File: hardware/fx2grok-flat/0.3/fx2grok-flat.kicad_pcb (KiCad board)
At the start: 4 copper layers, 34.9 x 16 mm, 36 parts, among them IC1 CY7C68013A-56, J1 Conn, P1 pkl_USB_OTG, U1 3.3V, U2 USBLC6-2, U3 IP425x-4-TTL, U4 IP425x-4-TTL, U5 24LC00, U6 IP425x-4-TTL, X1 24MHz

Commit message: Added 3d models to the board file.
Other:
- board text added: "1BitSquared"

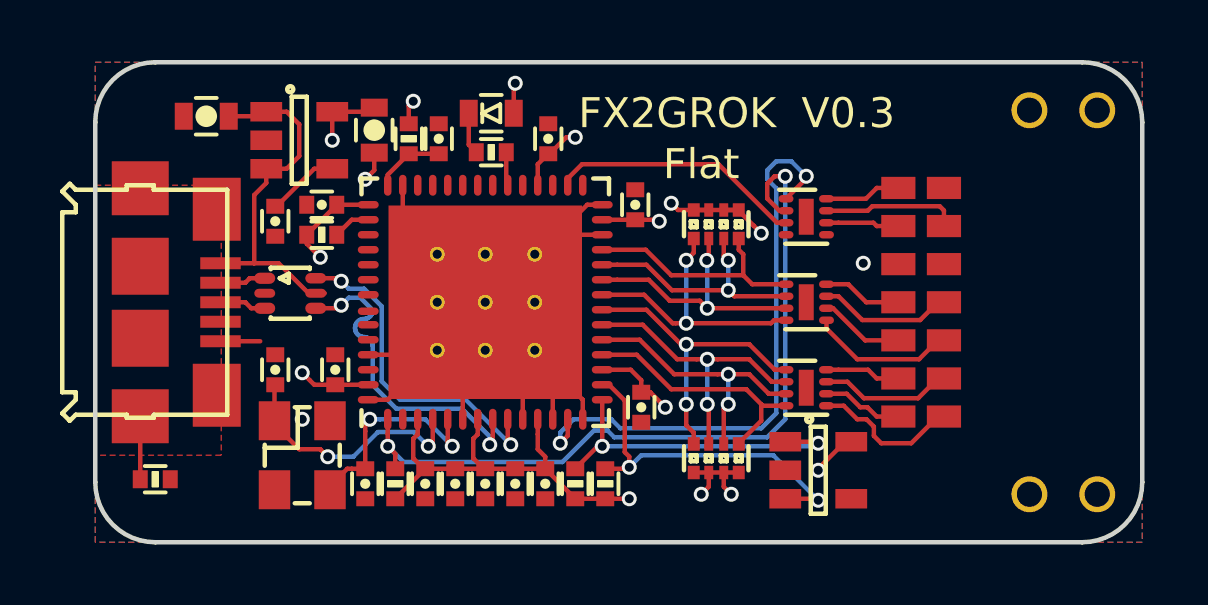
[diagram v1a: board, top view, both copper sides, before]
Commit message: Moved config flash to clean up PB0 trace.
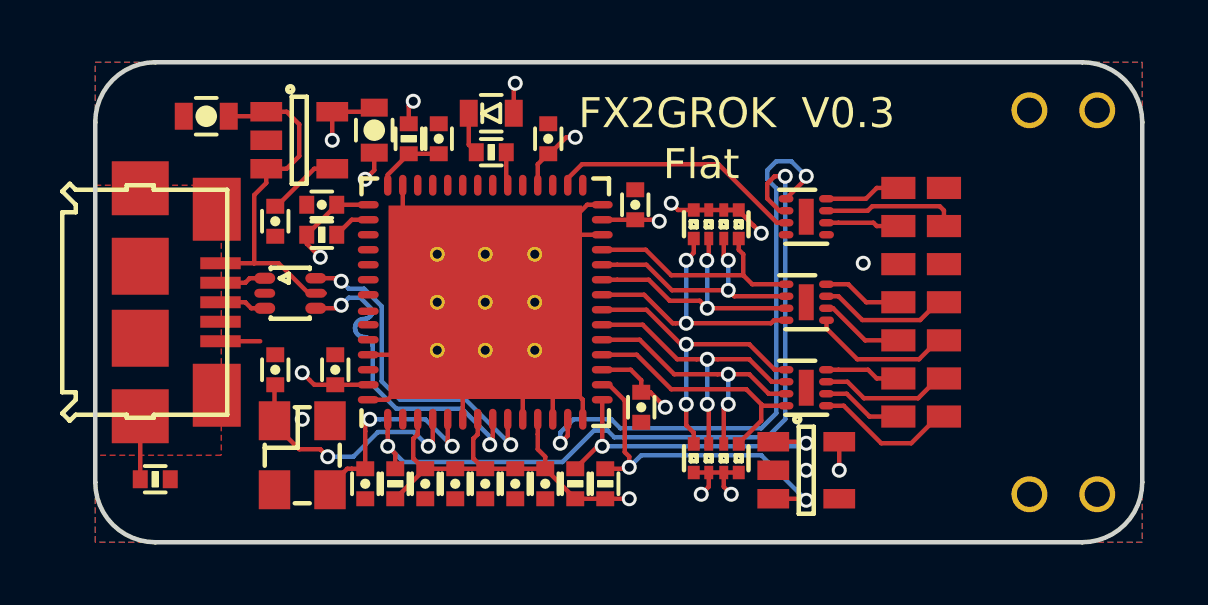
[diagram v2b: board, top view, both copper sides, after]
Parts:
- added REF**: 1b2_Logo_SilkS_10mm, pkl_logos:1b2_Logo_SilkS_10mm, B.Cu at (39.5, 30.5)
- moved U5 0.40 mm to (45.7, 35.6)
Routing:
- net +3V3: track 40.7 -> 40.1 mm
- net GND: vias 3 -> 4
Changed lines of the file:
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@@
-(kicad_pcb (version 20171130) (host pcbnew 5.0.0-rc2-dev-unknown-0d8692d~64~ubuntu16.04.1)
+(kicad_pcb (version 20171130) (host pcbnew 5.0.0-rc2-dev-unknown-268aeeb~64~ubuntu16.04.1)
   (general
     (thickness 1.6)
     (drawings 46)
-    (tracks 438)
+    (tracks 431)
     (zones 0)
-    (modules 36)
+    (modules 37)
     (nets 62)
   )
@@
     (add_net "Net-(U5-Pad4)")
   )
+  (module pkl_logos:1b2_Logo_SilkS_10mm locked (layer B.Cu)
+    (at 39.5 30.5 90)
+    (fp_text reference REF** (at 0 -6 90) (layer B.Fab)
+      (effects (font (size 1 1) (thickness 0.15)) (justify mirror))
+    )
+    (fp_text value 1b2_Logo_SilkS_10mm (at 0 6.35 90) (layer B.Fab)
+      (effects (font (size 1 1) (thickness 0.15)) (justify mirror))
+    )
+    (fp_line (start -1 1) (end -1 5) (layer B.SilkS) (width 0.4))
+    (fp_line (start -1 5) (end -5 5) (layer B.SilkS) (width 0.4))
+    (fp_line (start -5 5) (end -5 1) (layer B.SilkS) (width 0.4))
+    (fp_line (start -5 1) (end -1 1) (layer B.SilkS) (width 0.4))
+    (fp_line (start -1 5) (end 0 4) (layer B.SilkS) (width 0.4))
+    (fp_line (start 0 4) (end 0 0) (layer B.SilkS) (width 0.4))
+    (fp_line (start 0 0) (end -1 1) (layer B.SilkS) (width 0.4))
+    (fp_line (start -5 1) (end -4 0) (layer B.SilkS) (width 0.4))
+    (fp_line (start -4 0) (end 0 0) (layer B.SilkS) (width 0.4))
+    (fp_line (start 4 4) (end 1 4) (layer B.SilkS) (width 0.4))
+    (fp_line (start 1 4) (end 1 -1) (layer B.SilkS) (width 0.4))
+    (fp_line (start 1 -1) (end -4 -1) (layer B.SilkS) (width 0.4))
+    (fp_line (start -4 -1) (end -4 -4) (layer B.SilkS) (width 0.4))
+    (fp_line (start -4 -4) (end 4 -4) (layer B.SilkS) (width 0.4))
+    (fp_line (start 4 -4) (end 4 4) (layer B.SilkS) (width 0.4))
+    (fp_line (start 4 4) (end 5 3) (layer B.SilkS) (width 0.4))
+    (fp_line (start 5 3) (end 5 -5) (layer B.SilkS) (width 0.4))
+    (fp_line (start 5 -5) (end 4 -4) (layer B.SilkS) (width 0.4))
+    (fp_line (start -4 -4) (end -3 -5) (layer B.SilkS) (width 0.4))
+    (fp_line (start -3 -5) (end 5 -5) (layer B.SilkS) (width 0.4))
+  )
   (module pkl_samtec:TFM-107-02-x-DH locked (layer F.Cu)
     (at 55.4 30 270)
@@
   )
   (module pkl_housings_sot:SOT-23-5 (layer F.Cu)
-    (at 46.1 35.6 180)
+    (at 45.7 35.6 180)
     (descr "5-pin SOT23 package")
     (tags SOT-23-5)
@@
   (segment (start 42.45 26.925) (end 41.425004 26.925) (width 0.15) (layer F.Cu) (net 1))
   (via (at 41.200004 26.7) (size 0.5) (drill 0.3) (layers F.Cu B.Cu) (net 1))
-  (segment (start 47.2 34.65) (end 46.995 34.65) (width 0.15) (layer F.Cu) (net 1))
-  (segment (start 46.995 34.65) (end 46.1 35.545) (width 0.15) (layer F.Cu) (net 1))
-  (segment (start 46.1 35.545) (end 46.1 35.6) (width 0.15) (layer F.Cu) (net 1))
-  (via (at 46.1 35.6) (size 0.5) (drill 0.3) (layers F.Cu B.Cu) (net 1))
   (segment (start 39 36.55) (end 39.8 36.55) (width 0.15) (layer F.Cu) (net 1))
   (via (at 39.8 36.55) (size 0.5) (drill 0.3) (layers F.Cu B.Cu) (net 1))
@@
   (segment (start 35.95 22.75) (end 36 22.7) (width 0.15) (layer F.Cu) (net 1))
   (segment (start 35.95 23.7) (end 35.95 22.75) (width 0.15) (layer F.Cu) (net 1))
+  (via (at 46.8 35.6) (size 0.5) (drill 0.3) (layers F.Cu B.Cu) (net 1))
+  (segment (start 46.8 34.65) (end 46.8 35.6) (width 0.15) (layer F.Cu) (net 1))
   (segment (start 31.3 25.013544) (end 31.3 25.6) (width 0.15) (layer F.Cu) (net 2))
   (segment (start 31.3 25.6) (end 31 25.9) (width 0.15) (layer F.Cu) (net 2))
@@
   (via (at 47.6 28.7) (size 0.5) (drill 0.3) (layers F.Cu B.Cu) (net 2))
   (via (at 28.9 33.9) (size 0.5) (drill 0.3) (layers F.Cu B.Cu) (net 2))
+  (via (at 45.7 35.6) (size 0.5) (drill 0.3) (layers F.Cu B.Cu) (net 2))
   (segment (start 26.175 28.7) (end 27.3 28.7) (width 0.15) (layer F.Cu) (net 3))
   (segment (start 27.3 28.7) (end 28.110715 28.7) (width 0.15) (layer F.Cu) (net 3))
@@
   (segment (start 33.75 33.9) (end 33.75 34.650002) (width 0.15) (layer F.Cu) (net 6))
   (via (at 33.899998 34.8) (size 0.5) (drill 0.3) (layers F.Cu B.Cu) (net 6))
-  (segment (start 45 34.65) (end 46.05 34.65) (width 0.15) (layer F.Cu) (net 7))
-  (segment (start 46.05 34.65) (end 46.1 34.7) (width 0.15) (layer F.Cu) (net 7))
-  (via (at 46.1 34.7) (size 0.5) (drill 0.3) (layers F.Cu B.Cu) (net 7))
+  (segment (start 44.6 34.65) (end 45.65 34.65) (width 0.15) (layer F.Cu) (net 7))
+  (segment (start 45.65 34.65) (end 45.7 34.7) (width 0.15) (layer F.Cu) (net 7))
+  (via (at 45.7 34.7) (size 0.5) (drill 0.3) (layers F.Cu B.Cu) (net 7))
   (segment (start 38.75 34.8) (end 38.9 34.8) (width 0.15) (layer F.Cu) (net 7))
   (segment (start 38.9 33.25) (end 38.9 34.8) (width 0.15) (layer F.Cu) (net 7))
   (via (at 38.9 34.8) (size 0.5) (drill 0.3) (layers F.Cu B.Cu) (net 7))
-  (segment (start 46 34.8) (end 38.9 34.8) (width 0.15) (layer B.Cu) (net 7))
-  (segment (start 46.1 34.7) (end 46 34.8) (width 0.15) (layer B.Cu) (net 7))
   (segment (start 38 35.55) (end 38.75 34.8) (width 0.15) (layer F.Cu) (net 7))
-  (segment (start 46.1 36.6) (end 44.6 35.1) (width 0.15) (layer B.Cu) (net 8))
-  (segment (start 44.6 35.1) (end 40.2 35.1) (width 0.15) (layer B.Cu) (net 8))
-  (segment (start 40.2 35.1) (end 39.8 35.5) (width 0.15) (layer B.Cu) (net 8))
-  (segment (start 45 36.55) (end 46.05 36.55) (width 0.15) (layer F.Cu) (net 8))
-  (segment (start 46.05 36.55) (end 46.1 36.6) (width 0.15) (layer F.Cu) (net 8))
-  (via (at 46.1 36.6) (size 0.5) (drill 0.3) (layers F.Cu B.Cu) (net 8))
+  (segment (start 45.6 34.8) (end 45.7 34.7) (width 0.15) (layer B.Cu) (net 7))
+  (segment (start 38.9 34.8) (end 45.6 34.8) (width 0.15) (layer B.Cu) (net 7))
+  (segment (start 44.6 36.55) (end 45.65 36.55) (width 0.15) (layer F.Cu) (net 8))
+  (via (at 45.7 36.6) (size 0.5) (drill 0.3) (layers F.Cu B.Cu) (net 8))
   (segment (start 39 35.55) (end 39.75 35.55) (width 0.15) (layer F.Cu) (net 8))
   (segment (start 39.75 35.55) (end 39.8 35.5) (width 0.15) (layer F.Cu) (net 8))
@@
   (segment (start 39.8 35.146447) (end 39.8 35.5) (width 0.15) (layer F.Cu) (net 8))
   (via (at 39.8 35.5) (size 0.5) (drill 0.3) (layers F.Cu B.Cu) (net 8))
+  (segment (start 45.65 36.55) (end 45.7 36.6) (width 0.15) (layer F.Cu) (net 8))
+  (segment (start 44.2 35.1) (end 45.7 36.6) (width 0.15) (layer B.Cu) (net 8))
+  (segment (start 40.2 35.1) (end 44.2 35.1) (width 0.15) (layer B.Cu) (net 8))
+  (segment (start 39.8 35.5) (end 40.2 35.1) (width 0.15) (layer B.Cu) (net 8))
   (segment (start 44.2 33.45) (end 44.2 33.4) (width 0.15) (layer F.Cu) (net 9))
   (segment (start 44.2 33.4) (end 43.7 32.9) (width 0.15) (layer F.Cu) (net 9))
@@
   (segment (start 41.95 28.35) (end 41.7 28.6) (width 0.15) (layer F.Cu) (net 18))
   (via (at 41.7 28.6) (size 0.5) (drill 0.3) (layers F.Cu B.Cu) (net 18))
-  (segment (start 47.74 33.5) (end 47.5 33.5) (width 0.15) (layer F.Cu) (net 19))
-  (segment (start 48.05 33.81) (end 47.74 33.5) (width 0.15) (layer F.Cu) (net 19))
   (segment (start 47.05 33.05) (end 46.375 33.05) (width 0.15) (layer F.Cu) (net 19))
-  (segment (start 47.5 33.5) (end 47.05 33.05) (width 0.15) (layer F.Cu) (net 19))
-  (segment (start 48.77 33.81) (end 48.05 33.81) (width 0.15) (layer F.Cu) (net 19))
+  (segment (start 47.81 33.81) (end 47.05 33.05) (width 0.15) (layer F.Cu) (net 19))
+  (segment (start 48.77 33.81) (end 47.81 33.81) (width 0.15) (layer F.Cu) (net 19))
+  (segment (start 46.375 33.45) (end 46.95 33.45) (width 0.15) (layer F.Cu) (net 20))
+  (segment (start 49.2 34.7) (end 50.09 33.81) (width 0.15) (layer F.Cu) (net 20))
   (segment (start 50.09 33.81) (end 50.29 33.81) (width 0.15) (layer F.Cu) (net 20))
+  (segment (start 46.95 33.45) (end 48.2 34.7) (width 0.15) (layer F.Cu) (net 20))
   (segment (start 48.2 34.7) (end 49.2 34.7) (width 0.15) (layer F.Cu) (net 20))
-  (segment (start 47.954001 34.454001) (end 48.2 34.7) (width 0.15) (layer F.Cu) (net 20))
-  (segment (start 47.954001 34.145799) (end 47.954001 34.454001) (width 0.15) (layer F.Cu) (net 20))
-  (segment (start 49.2 34.7) (end 50.09 33.81) (width 0.15) (layer F.Cu) (net 20))
-  (segment (start 46.375 33.45) (end 46.95 33.45) (width 0.15) (layer F.Cu) (net 20))
-  (segment (start 46.95 33.45) (end 47.4 33.9) (width 0.15) (layer F.Cu) (net 20))
-  (segment (start 47.4 33.9) (end 47.708202 33.9) (width 0.15) (layer F.Cu) (net 20))
-  (segment (start 47.708202 33.9) (end 47.954001 34.145799) (width 0.15) (layer F.Cu) (net 20))
   (segment (start 46.775 32.25) (end 46.375 32.25) (width 0.15) (layer F.Cu) (net 21))
   (segment (start 47.76 32.25) (end 46.775 32.25) (width 0.15) (layer F.Cu) (net 21))

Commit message: Untangled the TRIG and IFCLK traces.
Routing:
- net /IFCLK: track 19.9 -> 17.2 mm
- net /TRIG: track 26.1 -> 25.3 mm
- net GND: vias 4 -> 8
- net (no net): vias 0 -> 1
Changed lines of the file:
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@@
     (thickness 1.6)
     (drawings 46)
-    (tracks 431)
+    (tracks 424)
     (zones 0)
     (modules 37)
@@
     (34 B.Paste user)
     (35 F.Paste user)
-    (36 B.SilkS user)
+    (36 B.SilkS user hide)
     (37 F.SilkS user)
     (38 B.Mask user)
@@
   (segment (start 32.25 27.25) (end 32.58125 27.58125) (width 0.15) (layer F.Cu) (net 2))
   (segment (start 26.175 31.3) (end 27.5 31.3) (width 0.15) (layer F.Cu) (net 2))
-  (via (at 47.6 28.7) (size 0.5) (drill 0.3) (layers F.Cu B.Cu) (net 2))
+  (via (at 47.5 28.7) (size 0.5) (drill 0.3) (layers F.Cu B.Cu) (net 2))
   (via (at 28.9 33.9) (size 0.5) (drill 0.3) (layers F.Cu B.Cu) (net 2))
   (via (at 45.7 35.6) (size 0.5) (drill 0.3) (layers F.Cu B.Cu) (net 2))
+  (via (at 45.7 31.4) (size 0.5) (drill 0.3) (layers F.Cu B.Cu) (net 2))
+  (via (at 45.7 34) (size 0.5) (drill 0.3) (layers F.Cu B.Cu) (net 2))
+  (via (at 45.7 28.6) (size 0.5) (drill 0.3) (layers F.Cu B.Cu) (net 2))
   (segment (start 26.175 28.7) (end 27.3 28.7) (width 0.15) (layer F.Cu) (net 3))
   (segment (start 27.3 28.7) (end 28.110715 28.7) (width 0.15) (layer F.Cu) (net 3))
@@
   (via (at 31.75 34.8) (size 0.5) (drill 0.3) (layers F.Cu B.Cu) (net 33))
   (segment (start 31.75 34.4) (end 31.75 33.9) (width 0.15) (layer F.Cu) (net 33))
-  (via (at 45 25.8) (size 0.5) (drill 0.3) (layers F.Cu B.Cu) (net 33))
-  (segment (start 31.999999 35.049999) (end 31.75 34.8) (width 0.15) (layer B.Cu) (net 33))
-  (segment (start 32.275999 35.325999) (end 31.999999 35.049999) (width 0.15) (layer B.Cu) (net 33))
-  (segment (start 37.574001 35.325999) (end 32.275999 35.325999) (width 0.15) (layer B.Cu) (net 33))
-  (segment (start 38.624001 34.275999) (end 37.574001 35.325999) (width 0.15) (layer B.Cu) (net 33))
-  (segment (start 39.077521 34.275999) (end 38.624001 34.275999) (width 0.15) (layer B.Cu) (net 33))
-  (segment (start 45 25.8) (end 45 33.9) (width 0.15) (layer B.Cu) (net 33))
-  (segment (start 44.399011 34.500989) (end 39.302511 34.500989) (width 0.15) (layer B.Cu) (net 33))
-  (segment (start 45 33.9) (end 44.399011 34.500989) (width 0.15) (layer B.Cu) (net 33))
-  (segment (start 39.302511 34.500989) (end 39.077521 34.275999) (width 0.15) (layer B.Cu) (net 33))
-  (segment (start 45 25.8) (end 44.646447 25.8) (width 0.15) (layer F.Cu) (net 33))
-  (segment (start 44.646447 25.8) (end 44.4 26.046447) (width 0.15) (layer F.Cu) (net 33))
-  (segment (start 44.806426 26.95) (end 45.025 26.95) (width 0.15) (layer F.Cu) (net 33))
-  (segment (start 44.4 26.543574) (end 44.806426 26.95) (width 0.15) (layer F.Cu) (net 33))
-  (segment (start 44.4 26.046447) (end 44.4 26.543574) (width 0.15) (layer F.Cu) (net 33))
+  (segment (start 44.806426 26.95) (end 44.1 26.243574) (width 0.15) (layer F.Cu) (net 33))
+  (segment (start 44.1 26.243574) (end 44.1 25.8) (width 0.15) (layer F.Cu) (net 33))
+  (segment (start 45.025 26.95) (end 44.806426 26.95) (width 0.15) (layer F.Cu) (net 33))
+  (via (at 44.1 25.8) (size 0.5) (drill 0.3) (layers F.Cu B.Cu) (net 33))
+  (segment (start 44.7 26.4) (end 44.1 25.8) (width 0.15) (layer B.Cu) (net 33))
+  (segment (start 44.7 33.5) (end 44.7 26.4) (width 0.15) (layer B.Cu) (net 33))
+  (segment (start 44.2 34) (end 44.7 33.5) (width 0.15) (layer B.Cu) (net 33))
+  (segment (start 31.75 34.8) (end 32.35 35.4) (width 0.15) (layer B.Cu) (net 33))
+  (segment (start 37.8 34) (end 44.2 34) (width 0.15) (layer B.Cu) (net 33))
+  (segment (start 32.35 35.4) (end 36.4 35.4) (width 0.15) (layer B.Cu) (net 33))
+  (segment (start 36.4 35.4) (end 37.8 34) (width 0.15) (layer B.Cu) (net 33))
   (segment (start 45.025 27.35) (end 44.724002 27.35) (width 0.15) (layer F.Cu) (net 34))
   (segment (start 37.75 25.875) (end 37.75 26.1) (width 0.15) (layer F.Cu) (net 34))
@@
   (segment (start 48.05 26.19) (end 47.69 26.55) (width 0.15) (layer F.Cu) (net 37))
   (segment (start 48.77 26.19) (end 48.05 26.19) (width 0.15) (layer F.Cu) (net 37))
-  (via (at 37.5 34.7) (size 0.5) (drill 0.3) (layers F.Cu B.Cu) (net 41))
-  (segment (start 37.75 34.45) (end 37.5 34.7) (width 0.15) (layer F.Cu) (net 41))
-  (segment (start 37.75 33.9) (end 37.75 34.45) (width 0.15) (layer F.Cu) (net 41))
-  (via (at 45.7 25.8) (size 0.5) (drill 0.3) (layers F.Cu B.Cu) (net 41))
-  (segment (start 45.7 25.875) (end 45.025 26.55) (width 0.15) (layer F.Cu) (net 41))
-  (segment (start 45.7 25.8) (end 45.7 25.875) (width 0.15) (layer F.Cu) (net 41))
-  (segment (start 45.2 25.3) (end 45.7 25.8) (width 0.15) (layer B.Cu) (net 41))
-  (segment (start 37.5 34.346447) (end 37.946447 33.9) (width 0.15) (layer B.Cu) (net 41))
-  (segment (start 37.946447 33.9) (end 39.2 33.9) (width 0.15) (layer B.Cu) (net 41))
-  (segment (start 44.7 26.2) (end 44.4 25.9) (width 0.15) (layer B.Cu) (net 41))
-  (segment (start 44.7 25.3) (end 45.2 25.3) (width 0.15) (layer B.Cu) (net 41))
-  (segment (start 37.5 34.7) (end 37.5 34.346447) (width 0.15) (layer B.Cu) (net 41))
-  (segment (start 44.7 33.7) (end 44.7 26.2) (width 0.15) (layer B.Cu) (net 41))
-  (segment (start 39.5 34.2) (end 44.2 34.2) (width 0.15) (layer B.Cu) (net 41))
-  (segment (start 44.2 34.2) (end 44.7 33.7) (width 0.15) (layer B.Cu) (net 41))
-  (segment (start 44.4 25.9) (end 44.4 25.6) (width 0.15) (layer B.Cu) (net 41))
-  (segment (start 39.2 33.9) (end 39.5 34.2) (width 0.15) (layer B.Cu) (net 41))
-  (segment (start 44.4 25.6) (end 44.7 25.3) (width 0.15) (layer B.Cu) (net 41))
+  (segment (start 37.75 34.75) (end 37.8 34.8) (width 0.15) (layer F.Cu) (net 41))
+  (segment (start 37.75 33.9) (end 37.75 34.75) (width 0.15) (layer F.Cu) (net 41))
+  (via (at 37.8 34.8) (size 0.5) (drill 0.3) (layers F.Cu B.Cu) (net 41))
+  (segment (start 44.4 34.3) (end 45 33.7) (width 0.15) (layer B.Cu) (net 41))
+  (segment (start 37.8 34.8) (end 38.3 34.3) (width 0.15) (layer B.Cu) (net 41))
+  (segment (start 38.3 34.3) (end 44.4 34.3) (width 0.15) (layer B.Cu) (net 41))
+  (segment (start 45.025 26.55) (end 45.025 25.825) (width 0.15) (layer F.Cu) (net 41))
+  (segment (start 45.025 25.825) (end 45 25.8) (width 0.15) (layer F.Cu) (net 41))
+  (via (at 45 25.8) (size 0.5) (drill 0.3) (layers F.Cu B.Cu) (net 41))
+  (segment (start 45 33.7) (end 45 25.8) (width 0.15) (layer B.Cu) (net 41))
   (segment (start 34.45 24.75) (end 34.7 25) (width 0.15) (layer F.Cu) (net 60))
   (segment (start 34.45 23.7) (end 34.45 24.75) (width 0.15) (layer F.Cu) (net 60))
+  (via (at 45.7 25.7) (size 0.5) (drill 0.3) (layers F.Cu B.Cu) (net 0))
+  (via (at 51.5 28.7) (size 0.5) (drill 0.3) (layers F.Cu B.Cu) (net 2))
   (zone (net 2) (net_name GND) (layer F.Cu) (hatch edge 0.508)
     (connect_pads (clearance 0.15))

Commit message: Added TRIG2 (RDY1/SLWR) as per @StefanBruens request. :D
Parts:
- added R7: 100k, pkl_dipol:R_0402, F.Cu at (33.0, 36.0)
- moved C1 1.00 mm to (38.0, 36.0)
- moved C10 1.00 mm to (36.0, 36.0)
- moved C7 1.00 mm to (34.0, 36.0)
- moved C8 1.00 mm to (37.0, 36.0)
- moved C9 1.00 mm to (35.0, 36.0)
- moved R2 1.00 mm to (39.0, 36.0)
- moved R3 1.00 mm to (40.0, 36.0)
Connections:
- IC1 pad 2: Net-(IC1-Pad2) -> /TRIG2
- J1 pad 13: Net-(J1-Pad13) -> /xTRIG2
- U6 pad 1: /IFCLK -> /TRIG2
- U6 pad 2: /TRIG -> /IFCLK
- U6 pad 3: /CLK -> /TRIG
- U6 pad 4: (no net) -> /CLK
- U6 pad 5: (no net) -> /xCLK
- U6 pad 6: /xCLK -> /xTRIG
- U6 pad 7: /xTRIG -> /xIFCLK
- U6 pad 8: /xIFCLK -> /xTRIG2
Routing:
- net /TRIG2: track 0.00 -> 26.4 mm, vias 0 -> 2
- net /xTRIG2: track 0.00 -> 4.94 mm
- net /USBD_N: track 11.2 -> 9.72 mm
- net /USBD_P: track 11.2 -> 9.78 mm
- net /TRIG: track 25.3 -> 26.7 mm
- net /IFCLK: track 17.2 -> 18.3 mm
- net +3V3: track 40.1 -> 40.8 mm
- net /SDA: track 11.9 -> 11.2 mm
- net /CLK: track 8.50 -> 9.10 mm
- net GND: vias 8 -> 9
